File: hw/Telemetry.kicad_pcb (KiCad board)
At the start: 4 copper layers, 100 x 82 mm, 126 parts, among them J102 BOOT0, J103 SPORT, J104 SBUS, J105 USB_B_Micro, J106 UART_EXP, J201 Conn_01x02, J301 Conn_01x02, J302 Conn_01x02, J401 Conn_01x02, J402 Conn_01x02, J403 Conn_01x02, J404 Conn_01x02, J405 Conn_01x02, J406 Conn_01x02, J407 Conn_01x02, J408 Conn_01x02, J409 SERVO_OUT, J410 AUDIO, Q201 AO3401A, Q202 AO3401A, Q203 IRLML6344TRPBF, Q204 IRLML6344TRPBF, Q401 IRLML6344TRPBF, Q402 IRLML6344TRPBF, Q403 IRLML6344TRPBF, Q404 CSD17306Q5A, Q405 IRLML6344TRPBF, Q406 IRLML6344TRPBF, Q407 IRLML6344TRPBF, Q408 CSD17306Q5A, SW101 SW_Push, U101 STM32F303CBx, U102 IS25LP032D, U201 AP1501-K5, U202 RT6200, U301 LP2985-5.0, U302 ACS770xCB-100U-PSF, U303 MCP6001-OT, U304 ACS770xCB-100U-PSF, U305 MCP6001-OT, U401 MCP1416, U402 MCP1416, U403 MCP4012-xxxxCH, U404 MCP6001-OT, X101 TXC-7C

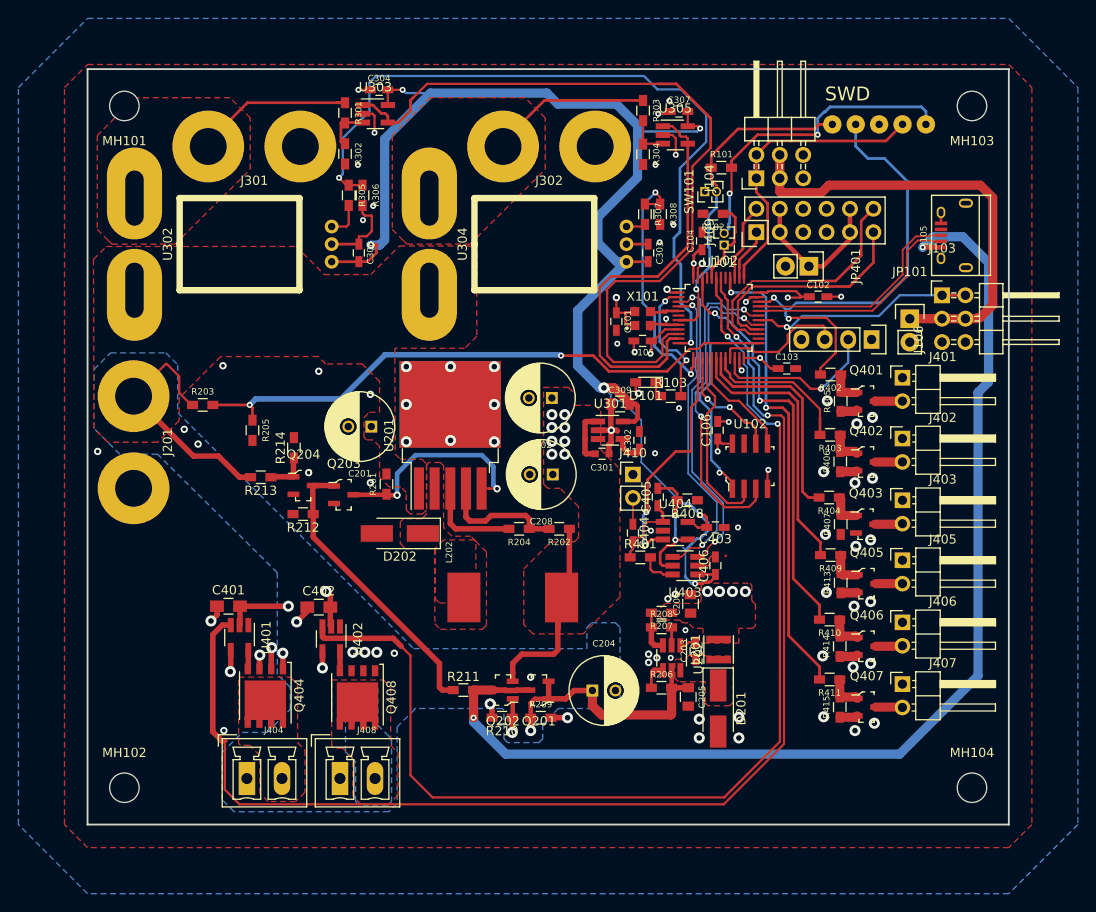
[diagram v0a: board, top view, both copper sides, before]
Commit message: Changed the digital potentiometer to AD5160 10k version and enabled SPI3
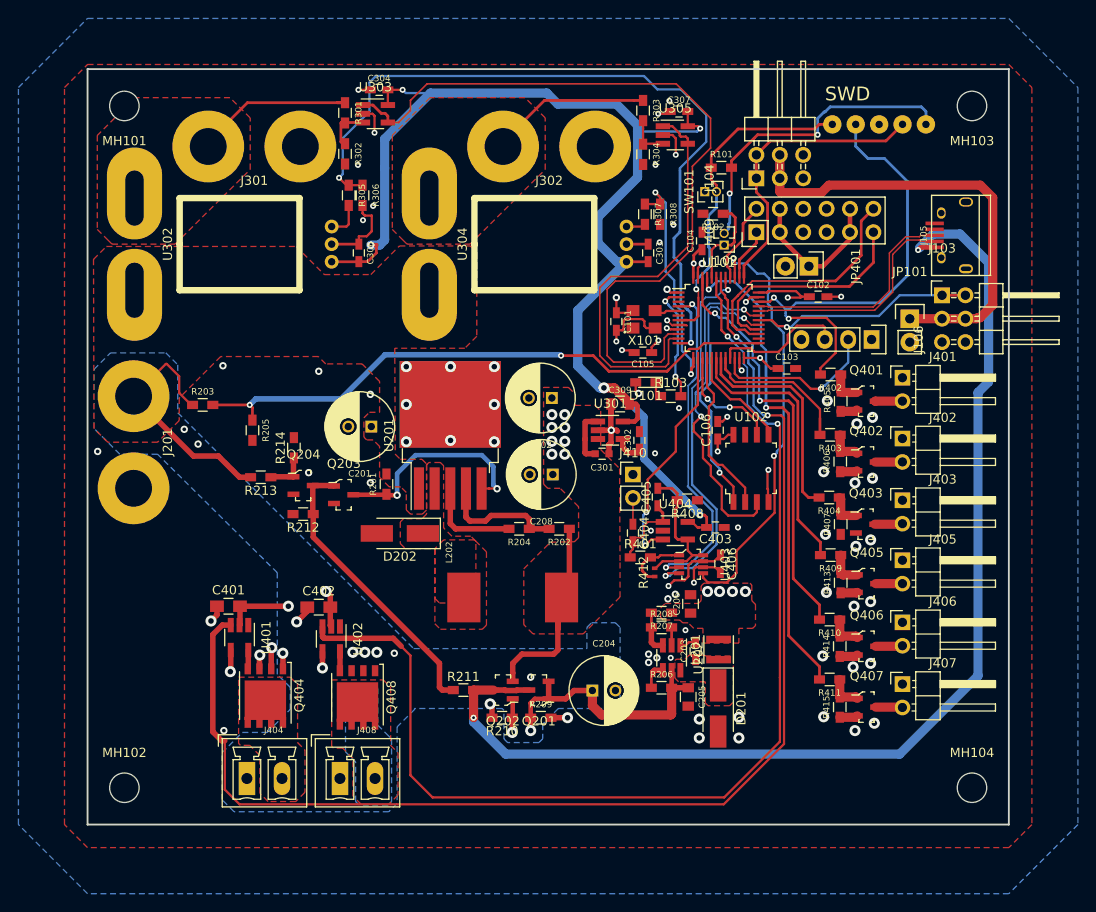
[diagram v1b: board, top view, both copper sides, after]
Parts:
- added R412: 0R, Resistors_SMD:R_0402_NoSilk, F.Cu at (121.6, 92.6)
- J105: footprint Connect:USB_Micro-B -> PCBDecals:USB_Micro-B
- U102: footprint digikey-footprints:SOIC-8_W3.9mm -> digikey-footprints:SOIC-8_W5.6mm
- U403: value MCP4012-xxxxCH -> AD5160BRJZ10-R2; footprint TO_SOT_Packages_SMD:SOT-23-6_Handsoldering -> digikey-footprints:SOT-23-8
- X101: value TXC-7C -> SG-310_SCF_8.000000MHZ; footprint PCBDecals:IQXO-791 -> PCBDecals:SG- 310
- moved C105 1.27 mm to (120.3, 68.8)
- moved U403 0.68 mm to (125.5, 91.7), turned to 270 degrees
- moved C406 0.58 mm to (128.7, 91.7), turned to 270 degrees
- moved U102 0.27 mm to (132.0, 81.3)
- moved X101 0.18 mm to (120.4, 65.2), turned to 0 degrees
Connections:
- C406 pad 1: +5VA -> VCC
- U101 pad 3: AMP_DIR -> (no net)
- U101 pad 39: SERVO_OUT2 -> AMP_CLK
- U101 pad 40: OUT6 -> SERVO_OUT2
- U101 pad 41: (no net) -> AMP_DIN
- U101 pad 45: (no net) -> OUT6
- U403 pad 1: +5VA -> Net-(C405-Pad2)
- U403 pad 2: GND -> VCC
- U403 pad 3: AMP_DIR -> GND
- U403 pad 4: AMP_CS -> AMP_CLK
- U403 pad 5: Net-(C405-Pad2) -> AMP_DIN
- U403 pad 6: Net-(R401-Pad2) -> AMP_CS
- X101 pad 1: +3V3 -> (no net)
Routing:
- net AMP_CLK: track 0.00 -> 46.8 mm, vias 0 -> 2
- net AMP_DIN: track 0.00 -> 41.3 mm, vias 0 -> 2
- net AMP_DIR: track 33.8 -> 0.00 mm, vias 2 -> 0
- net +5VA: track 150.8 -> 135.4 mm, vias 6 -> 5
- net GND: track 90.0 -> 98.2 mm, vias 85 -> 86
- net VCC: track 30.4 -> 38.2 mm, vias 8 -> 9
- net +3V3: track 66.7 -> 61.9 mm, vias 14 -> 15
- net AMP_CS: track 33.9 -> 36.8 mm
- net Net-(R401-Pad2): track 3.93 -> 6.74 mm
- net Net-(C405-Pad2): track 13.8 -> 16.4 mm, vias 2 -> 0
- net /SPI_MISO: track 20.6 -> 18.1 mm
- net OUT6: track 50.6 -> 52.6 mm
- net ESC2_CURRENT_OUT: track 28.0 -> 26.3 mm
- net /USB_D-: track 24.6 -> 25.9 mm
- net /USB_D+: track 24.6 -> 25.9 mm
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
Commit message: Refactored schematic net names
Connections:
- net SERVO_OUT1 renamed SERVO_1
- net SERVO_OUT2 renamed SERVO_2
- net SERVO_OUT3 renamed SERVO_3
- net SERVO_OUT4 renamed SERVO_4

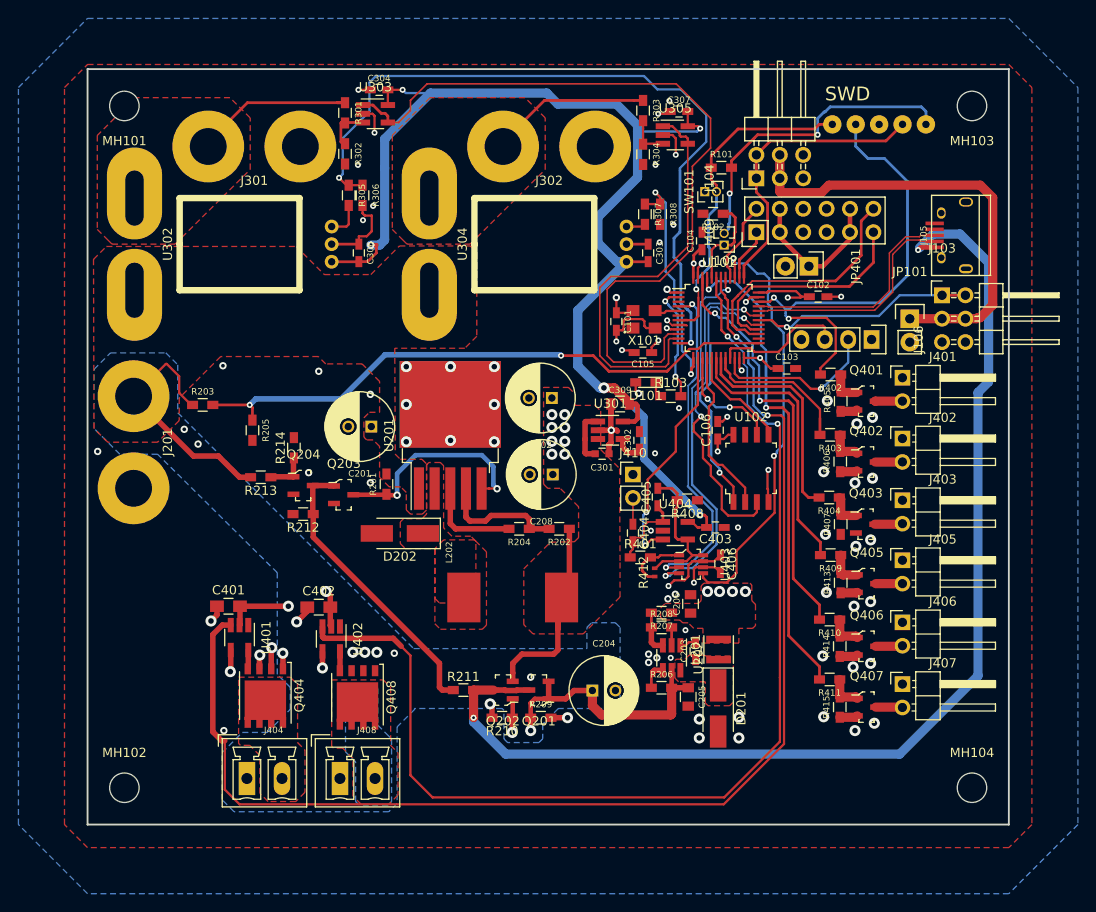
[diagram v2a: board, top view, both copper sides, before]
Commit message: Renamed schematic pdf Added gerbers Added layout pdf Fixed silkscreen on layout
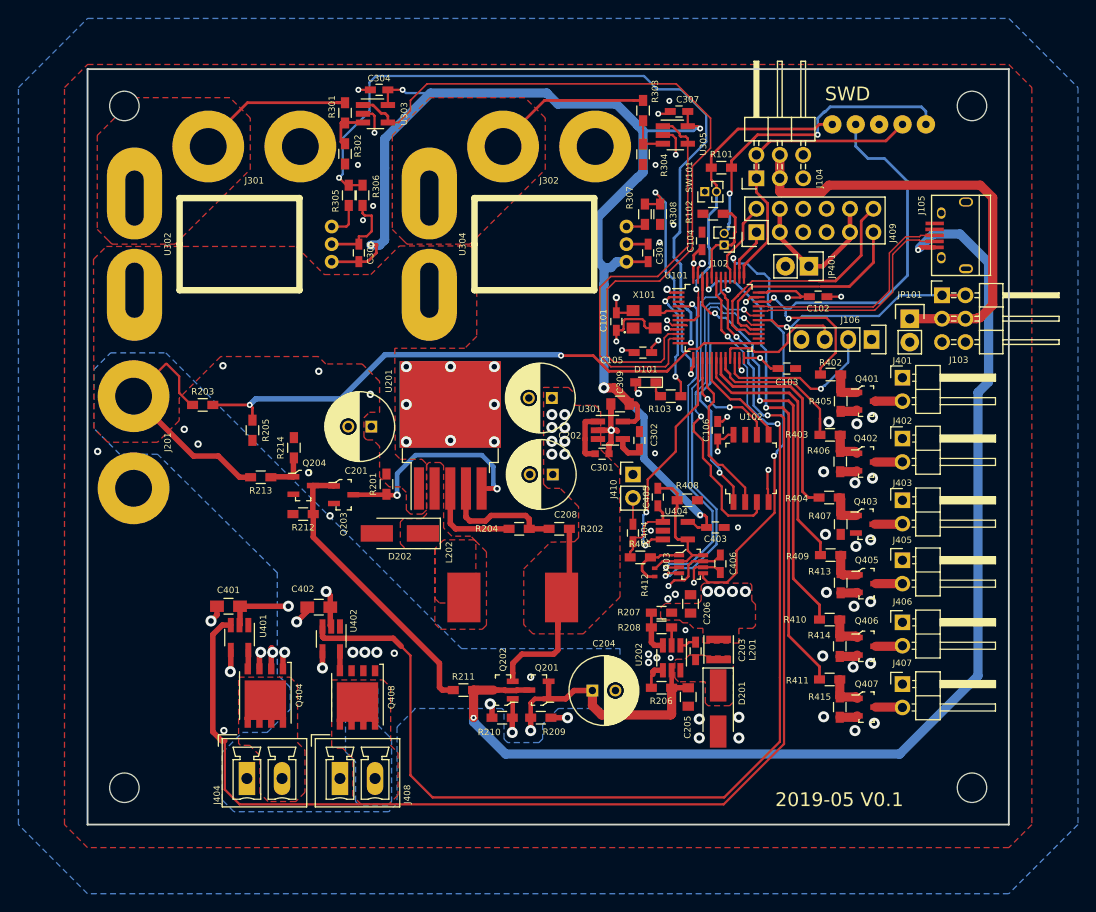
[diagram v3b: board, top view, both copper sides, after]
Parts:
- added REF***: OSHW-Symbol_13.4x12mm_SilkScreen, Symbols:OSHW-Symbol_13.4x12mm_SilkScreen, B.Cu at (67.7, 105.0)
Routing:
- net +5VA: track 135.4 -> 132.8 mm
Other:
- board text added: "2019-05 V0.1"
- board text added: "https://github.com/findersee/rctelemetry"

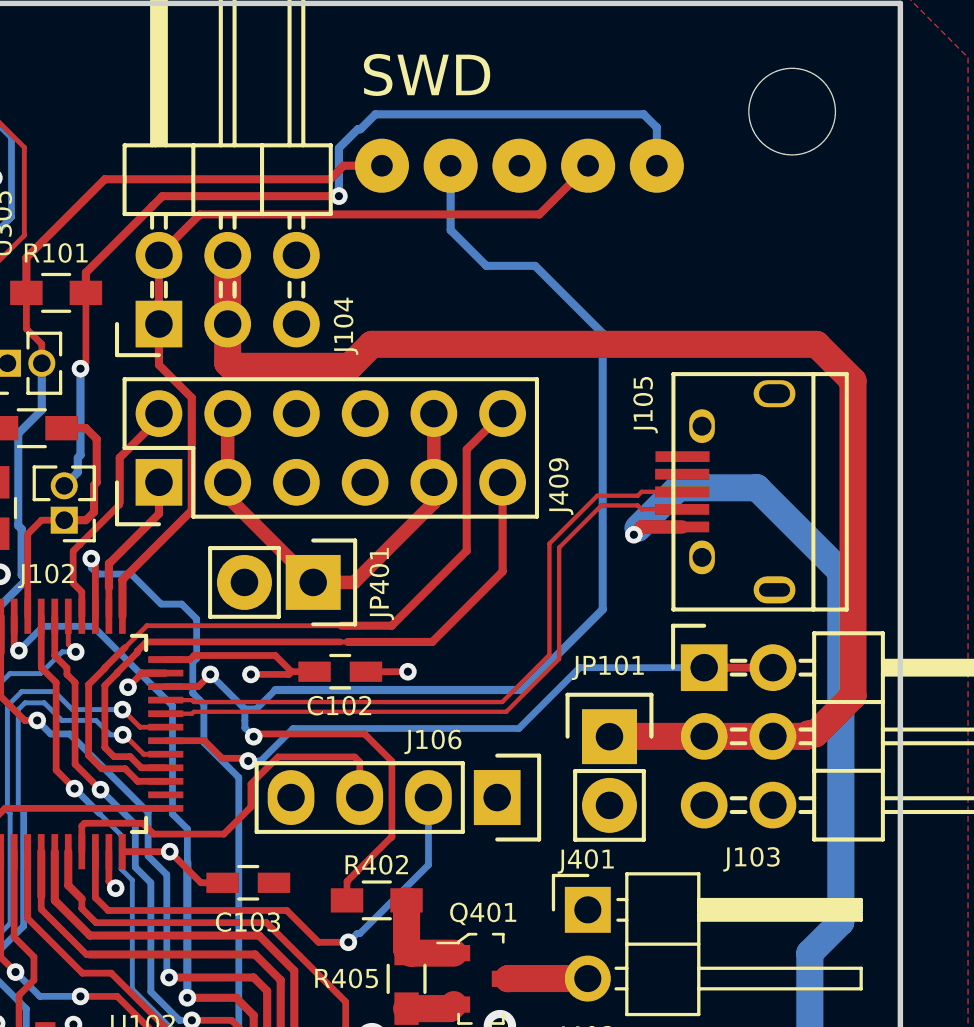
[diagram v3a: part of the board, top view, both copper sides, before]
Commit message: Added cooling temperature sensor
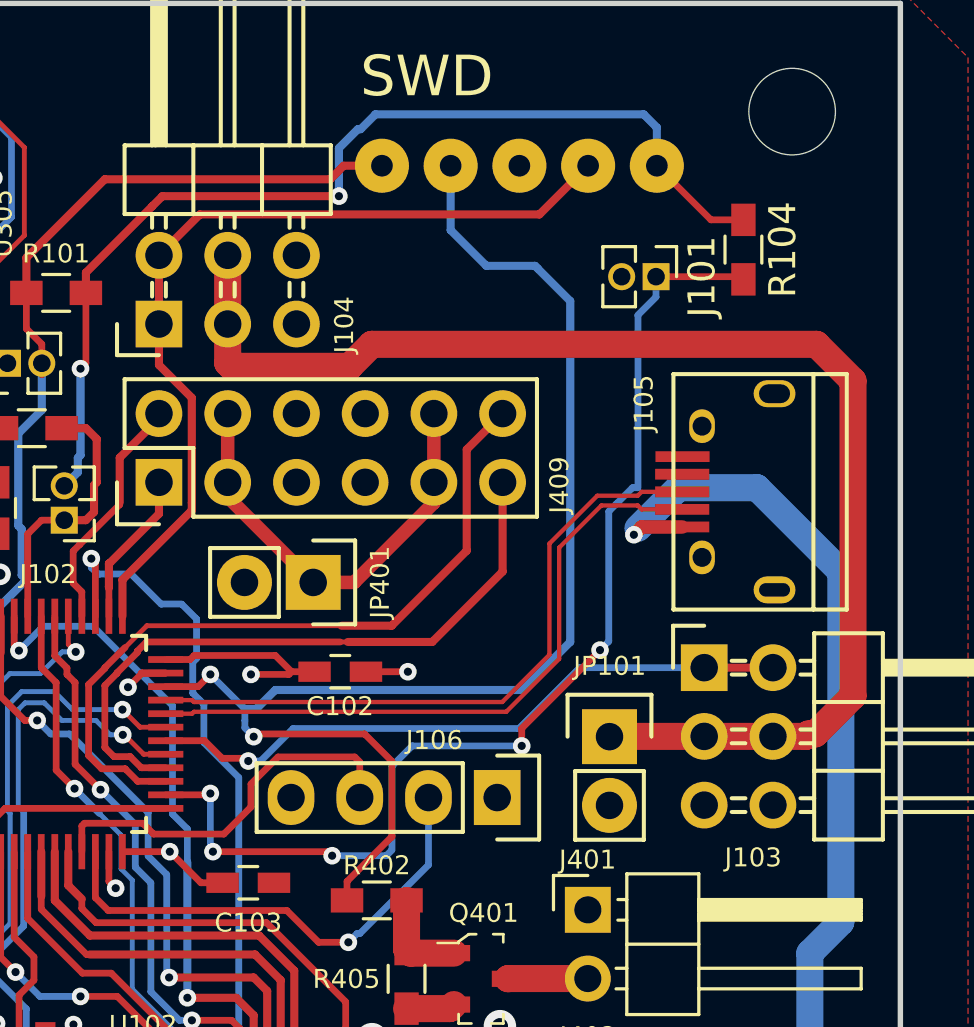
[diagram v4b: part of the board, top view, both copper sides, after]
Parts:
- added J101: BOOT0, Pin_Headers:Pin_Header_Straight_1x02_Pitch1.27mm, F.Cu at (151.0, 48.1)
- added R104: 10k, Resistors_SMD:R_0603_HandSoldering, F.Cu at (154.2, 47.1)
- C304: value C_Small -> 100n
- D201, D202: value D_Schottky -> SS54
- L201: value 4u7 -> SPN30304R7MPTE
- L202: value 47u -> BCRH1212Y-680M
- R405, R406, R407, R413, R414, R415: value R_Small -> 10k
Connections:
- U101 pad 26: (no net) -> COOLING_TEMP
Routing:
- net COOLING_TEMP: track 0.00 -> 41.6 mm, vias 0 -> 5
- net +3V3: track 61.9 -> 66.0 mm
- net OUT1: track 50.8 -> 49.8 mm
